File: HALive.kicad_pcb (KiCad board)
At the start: 2 copper layers, 58.4 x 88.9 mm, 14 parts, among them J1 Screw_Terminal_01x08, J2 Conn_01x06_Male, J3 Conn_01x02_Male, J4 Screw_Terminal_01x08, J6 Conn_01x02_Male, U1 MAX233, U2 TMR_1-1211, U3 LM358

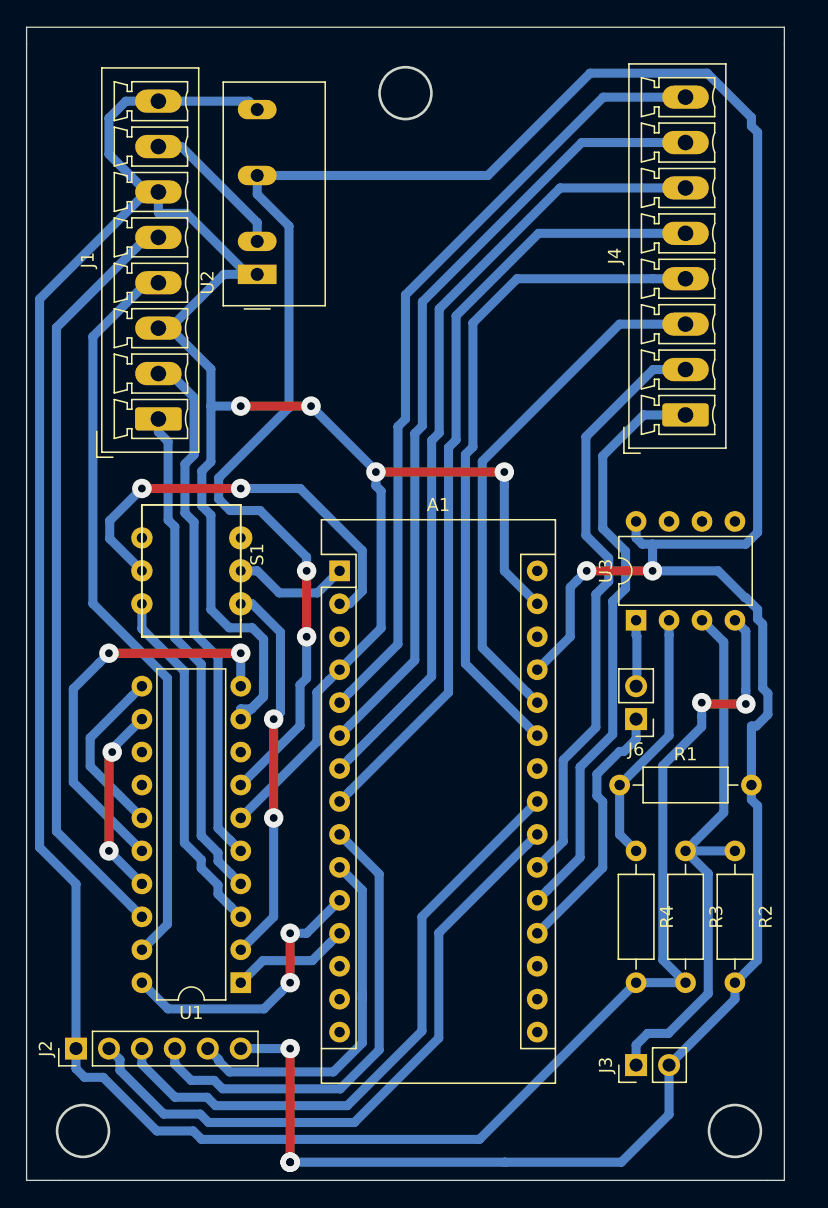
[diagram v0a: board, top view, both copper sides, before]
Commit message: added BEM280 sensor
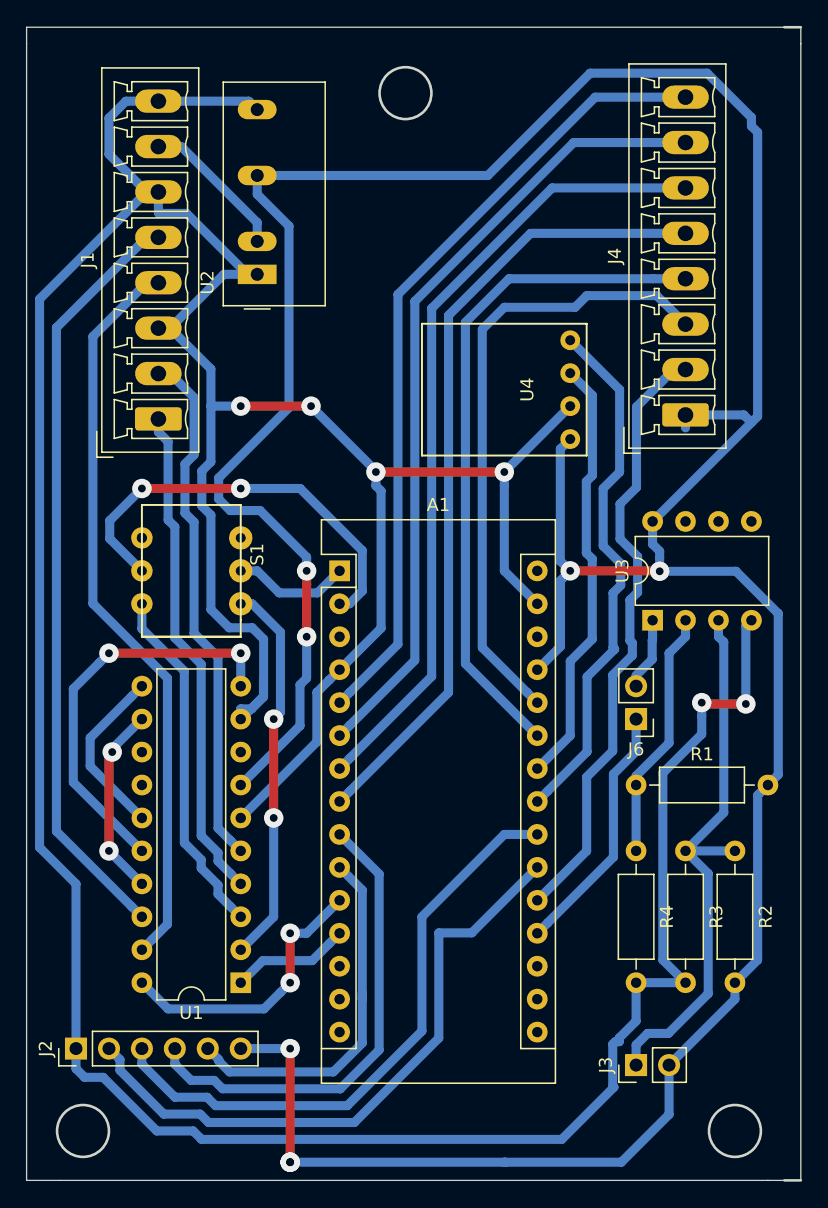
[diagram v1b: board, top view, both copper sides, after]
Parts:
- added U4: BME280, lorenzo2018:BME280, F.Cu at (74.9, 53.3)
- moved U3 1.27 mm to (85.1, 71.1)
- moved R1 1.27 mm to (83.8, 83.8)
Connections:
- A1 pad 21: /ANAIN2 -> Net-(A1-Pad21)
- A1 pad 23: Net-(A1-Pad23) -> /SDA
- A1 pad 24: Net-(A1-Pad24) -> /SCL
- J2 pad 2: Net-(A1-Pad22) -> Net-(A1-Pad21)
- J2 pad 3: Net-(A1-Pad23) -> Net-(A1-Pad22)
- J4 pad 1: /ANAIN1 -> +5V
- J4 pad 2: /ANAIN2 -> /ANAIN1
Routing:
- net Net-(A1-Pad21): track 0.00 -> 48.8 mm
- net Net-(A1-Pad23): track 47.9 -> 0.00 mm
- net /ANAIN2: track 46.0 -> 0.00 mm
- net /SDA: track 0.00 -> 41.0 mm
- net /SCL: track 0.00 -> 33.3 mm
- net +5V: track 256.2 -> 268.2 mm
- net GND: track 308.1 -> 319.1 mm
- net Net-(A1-Pad26): track 40.4 -> 48.2 mm
- net Net-(A1-Pad22): track 49.8 -> 46.8 mm
- net /ANAIN1: track 45.5 -> 47.5 mm
- net Net-(A1-Pad19): track 20.2 -> 19.7 mm
- net Net-(J6-Pad2): track 5.13 -> 5.69 mm
- net Net-(R1-Pad1): track 19.9 -> 19.4 mm
- net Net-(J3-Pad1): track 44.0 -> 43.5 mm
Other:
- board size 58.4 x 88.9 mm -> 59.7 x 88.9 mm

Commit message: pcb tweaks
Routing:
- net GND: track 319.1 -> 291.0 mm, vias 6 -> 10
- net Net-(A1-Pad22): track 46.8 -> 45.3 mm
- net Net-(A1-Pad21): track 48.8 -> 47.6 mm
- net /SDA: track 41.0 -> 40.0 mm
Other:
- board size 59.7 x 88.9 mm -> 58.4 x 88.9 mm
